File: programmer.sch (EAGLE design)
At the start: 20 parts, among them IC1 74ABT125DB, U1 ATMEGA8U2, X1 16MHz

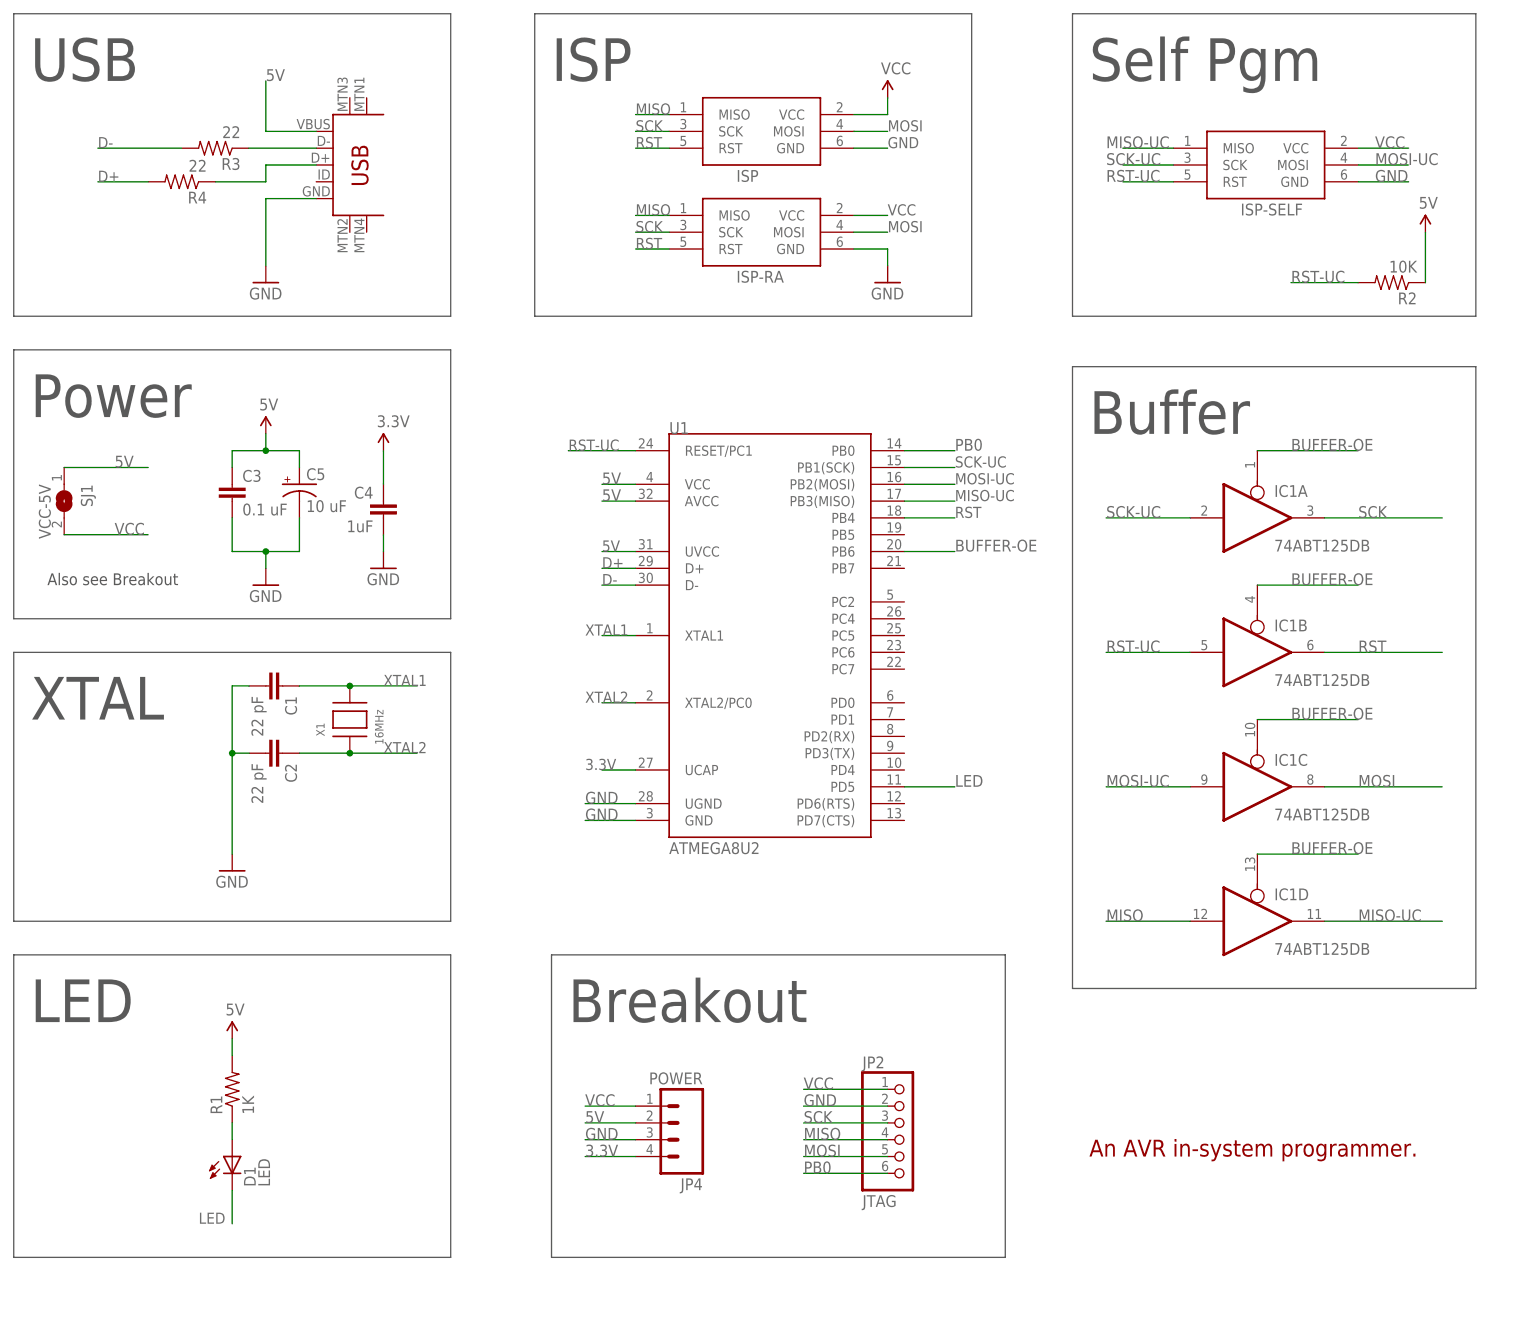
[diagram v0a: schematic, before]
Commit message: Resolved conflicts with dgentry's optimizations.
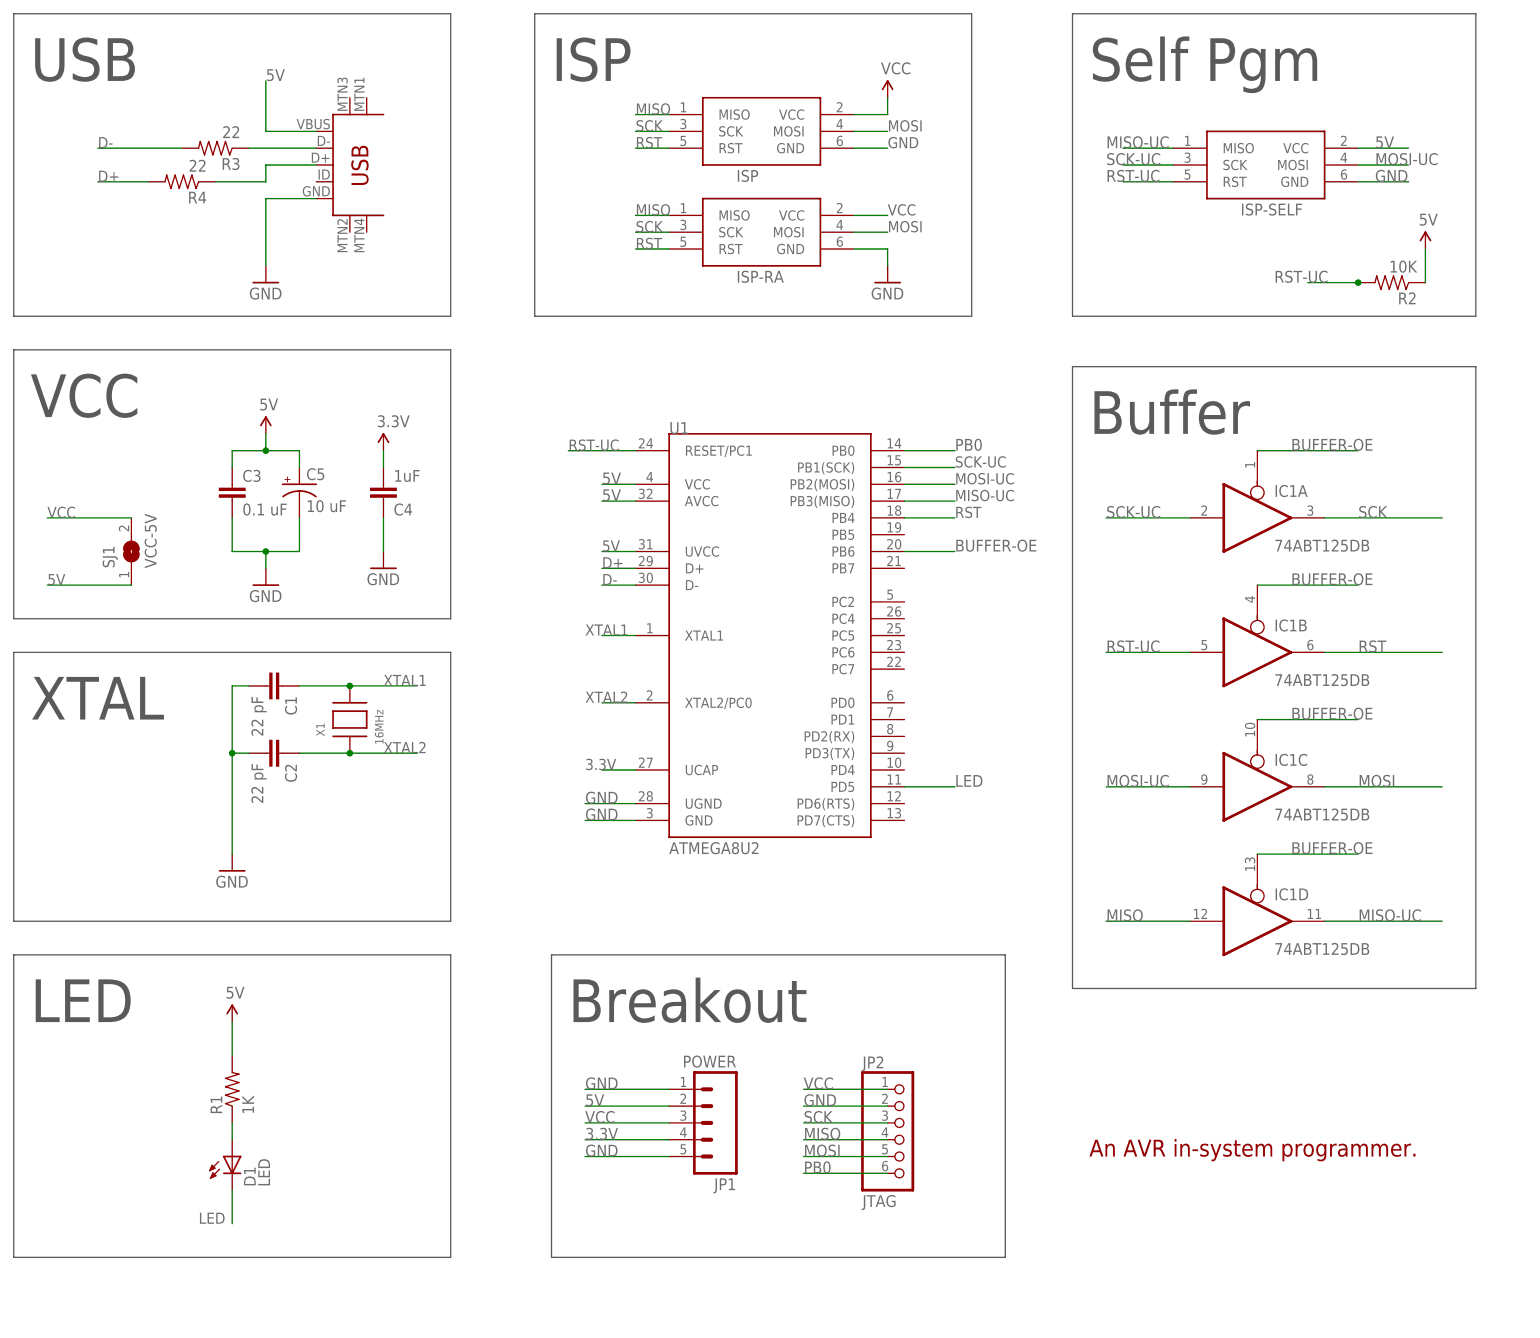
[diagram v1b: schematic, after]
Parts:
- removed JP4: POWER, SparkFun:M04PTH
- added JP1: POWER, SparkFun:M05PTH
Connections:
- net 3.3V: now also C4.2, JP1.4; no longer C4.1, JP4.4
- net 5V: now also ISP-SELF.VCC, JP1.2; no longer JP4.2
- net GND: now also C4.1, JP1.1, JP1.5; no longer C4.2, JP4.3
- net VCC: now also JP1.3; no longer ISP-SELF.VCC, JP4.1
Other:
- note added: "VCC"
- note removed: "Also see Breakout"
- note removed: "Power"
- moved on the sheet: C4, SJ1
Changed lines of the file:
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@@
 <part name="U$2" library="SparkFun" deviceset="5V" device=""/>
 <part name="U$3" library="SparkFun" deviceset="5V" device=""/>
-<part name="JP4" library="SparkFun" deviceset="M04" device="PTH" value="POWER"/>
+<part name="JP1" library="SparkFun" deviceset="M05" device="PTH" value="POWER"/>
 </parts>
 <sheets>
@@
 <wire x1="5.08" y1="48.26" x2="-60.96" y2="48.26" width="0.1524" layer="97"/>
 <wire x1="-60.96" y1="48.26" x2="-60.96" y2="88.9" width="0.1524" layer="97"/>
-<text x="-58.42" y="78.74" size="6.4516" layer="97" font="vector">Power</text>
+<text x="-58.42" y="78.74" size="6.4516" layer="97" font="vector">VCC</text>
 <wire x1="-60.96" y1="43.18" x2="5.08" y2="43.18" width="0.1524" layer="97"/>
 <wire x1="5.08" y1="43.18" x2="5.08" y2="2.54" width="0.1524" layer="97"/>
@@
 <wire x1="20.32" y1="-48.26" x2="20.32" y2="-2.54" width="0.1524" layer="97"/>
 <text x="22.86" y="-12.7" size="6.4516" layer="97" font="vector">Breakout</text>
-<text x="-55.88" y="53.34" size="1.778" layer="97" font="vector">Also see Breakout</text>
 </plain>
 <instances>
@@
 <instance part="R4" gate="G$1" x="-35.56" y="114.3" rot="R180"/>
 <instance part="R3" gate="G$1" x="-30.48" y="119.38" rot="R180"/>
-<instance part="C4" gate="G$1" x="-5.08" y="63.5" rot="MR0"/>
+<instance part="C4" gate="G$1" x="-5.08" y="68.58" rot="MR180"/>
 <instance part="R2" gate="G$1" x="147.32" y="99.06" rot="R180"/>
 <instance part="P+5" gate="G$1" x="-5.08" y="73.66"/>
@@
 <instance part="D1" gate="G$1" x="-27.94" y="-33.02"/>
 <instance part="R1" gate="G$1" x="-27.94" y="-22.86" rot="R90"/>
-<instance part="SJ1" gate="1" x="-53.34" y="66.04" rot="R270"/>
+<instance part="SJ1" gate="1" x="-43.18" y="58.42" rot="R90"/>
 <instance part="C5" gate="G$1" x="-17.78" y="68.58"/>
 <instance part="GND1" gate="1" x="-5.08" y="55.88"/>
@@
 <instance part="JP2" gate="A" x="73.66" y="-30.48"/>
 <instance part="U$1" gate="G$1" x="-22.86" y="76.2"/>
-<instance part="U$2" gate="G$1" x="-27.94" y="-15.24"/>
-<instance part="U$3" gate="G$1" x="152.4" y="106.68"/>
-<instance part="JP4" gate="G$1" x="38.1" y="-27.94" rot="R180"/>
+<instance part="U$2" gate="G$1" x="152.4" y="104.14"/>
+<instance part="U$3" gate="G$1" x="-27.94" y="-12.7"/>
+<instance part="JP1" gate="G$1" x="45.72" y="-27.94" rot="R180"/>
 </instances>
 <busses>
@@
 </segment>
 <segment>
+<wire x1="-55.88" y1="63.5" x2="-43.18" y2="63.5" width="0.1524" layer="91"/>
+<label x="-55.88" y="63.5" size="1.6764" layer="95" font="vector"/>
 <pinref part="SJ1" gate="1" pin="2"/>
-<wire x1="-40.64" y1="60.96" x2="-53.34" y2="60.96" width="0.1524" layer="91"/>
-<label x="-45.72" y="60.96" size="1.778" layer="95" font="vector"/>
-</segment>
-<segment>
-<pinref part="ISP-SELF" gate="G$1" pin="VCC"/>
-<wire x1="142.24" y1="119.38" x2="149.86" y2="119.38" width="0.1524" layer="91"/>
-<label x="144.78" y="119.38" size="1.778" layer="95" font="vector"/>
 </segment>
 <segment>
@@
 </segment>
 <segment>
+<wire x1="38.1" y1="-27.94" x2="25.4" y2="-27.94" width="0.1524" layer="91"/>
+<label x="25.4" y="-27.94" size="1.778" layer="95" font="vector"/>
+<pinref part="JP1" gate="G$1" pin="3"/>
+</segment>
+<segment>
 <pinref part="JP2" gate="A" pin="1"/>
 <wire x1="71.12" y1="-22.86" x2="58.42" y2="-22.86" width="0.1524" layer="91"/>
 <label x="58.42" y="-22.86" size="1.778" layer="95" font="vector"/>
-</segment>
-<segment>
-<pinref part="JP4" gate="G$1" pin="1"/>
-<wire x1="33.02" y1="-25.4" x2="25.4" y2="-25.4" width="0.1524" layer="91"/>
-<label x="25.4" y="-25.4" size="1.778" layer="95" font="vector"/>
 </segment>
 </net>
@@
 </segment>
 <segment>
-<pinref part="C4" gate="G$1" pin="2"/>
+<pinref part="C4" gate="G$1" pin="1"/>
 <pinref part="GND1" gate="1" pin="GND"/>
-<wire x1="-5.08" y1="60.96" x2="-5.08" y2="58.42" width="0.1524" layer="91"/>
+<wire x1="-5.08" y1="63.5" x2="-5.08" y2="58.42" width="0.1524" layer="91"/>
 </segment>
 <segment>
@@
 </segment>
 <segment>
-<pinref part="JP4" gate="G$1" pin="3"/>
-<wire x1="33.02" y1="-30.48" x2="25.4" y2="-30.48" width="0.1524" layer="91"/>
-<label x="25.4" y="-30.48" size="1.778" layer="95" font="vector"/>
-</segment>
-<segment>
+<wire x1="38.1" y1="-33.02" x2="25.4" y2="-33.02" width="0.1524" layer="91"/>
+<label x="25.4" y="-33.02" size="1.778" layer="95" font="vector"/>
+<wire x1="38.1" y1="-22.86" x2="25.4" y2="-22.86" width="0.1524" layer="91"/>
+<label x="25.4" y="-22.86" size="1.778" layer="95" font="vector"/>
+<pinref part="JP1" gate="G$1" pin="1"/>
+<pinref part="JP1" gate="G$1" pin="5"/>
+</segment>
+<segment>
+<pinref part="C5" gate="G$1" pin="-"/>
+<wire x1="-17.78" y1="58.42" x2="-17.78" y2="63.5" width="0.1524" layer="91"/>
 <pinref part="C3" gate="G$1" pin="2"/>
 <wire x1="-27.94" y1="63.5" x2="-27.94" y2="58.42" width="0.1524" layer="91"/>
-<pinref part="C5" gate="G$1" pin="-"/>
 <wire x1="-27.94" y1="58.42" x2="-22.86" y2="58.42" width="0.1524" layer="91"/>
+<pinref part="GND2" gate="1" pin="GND"/>
 <wire x1="-22.86" y1="58.42" x2="-17.78" y2="58.42" width="0.1524" layer="91"/>
-<wire x1="-17.78" y1="58.42" x2="-17.78" y2="63.5" width="0.1524" layer="91"/>
-<pinref part="GND2" gate="1" pin="GND"/>
 <wire x1="-22.86" y1="58.42" x2="-22.86" y2="55.88" width="0.1524" layer="91"/>
 <junction x="-22.86" y="58.42"/>
@@
 <net name="3.3V" class="0">
 <segment>
-<pinref part="C4" gate="G$1" pin="1"/>
+<pinref part="C4" gate="G$1" pin="2"/>
 <pinref part="P+5" gate="G$1" pin="3.3V"/>
-<wire x1="-5.08" y1="68.58" x2="-5.08" y2="73.66" width="0.1524" layer="91"/>
+<wire x1="-5.08" y1="71.12" x2="-5.08" y2="73.66" width="0.1524" layer="91"/>
 </segment>
 <segment>
@@
 </segment>
 <segment>
-<pinref part="JP4" gate="G$1" pin="4"/>
-<wire x1="33.02" y1="-33.02" x2="25.4" y2="-33.02" width="0.1524" layer="91"/>
-<label x="25.4" y="-33.02" size="1.778" layer="95" font="vector"/>
+<wire x1="38.1" y1="-30.48" x2="25.4" y2="-30.48" width="0.1524" layer="91"/>
+<label x="25.4" y="-30.48" size="1.778" layer="95" font="vector"/>
+<pinref part="JP1" gate="G$1" pin="4"/>
 </segment>
 </net>
@@
 </segment>
 <segment>
-<wire x1="-40.64" y1="71.12" x2="-53.34" y2="71.12" width="0.1524" layer="91"/>
+<label x="-55.88" y="53.34" size="1.6764" layer="95" font="vector"/>
+<wire x1="-55.88" y1="53.34" x2="-43.18" y2="53.34" width="0.1524" layer="91"/>
 <pinref part="SJ1" gate="1" pin="1"/>
-<label x="-45.72" y="71.12" size="1.778" layer="95" font="vector"/>
 </segment>
 <segment>
 <pinref part="U1" gate="G$1" pin="VCC"/>
 <wire x1="33.02" y1="68.58" x2="27.94" y2="68.58" width="0.1524" layer="91"/>
-<label x="27.94" y="68.58" size="1.778" layer="95"/>
+<label x="27.94" y="68.58" size="1.778" layer="95" font="vector"/>
 </segment>
 <segment>
 <pinref part="U1" gate="G$1" pin="AVCC"/>
 <wire x1="33.02" y1="66.04" x2="27.94" y2="66.04" width="0.1524" layer="91"/>
-<label x="27.94" y="66.04" size="1.778" layer="95"/>
+<label x="27.94" y="66.04" size="1.778" layer="95" font="vector"/>
 </segment>
 <segment>
@@
 <wire x1="-27.94" y1="71.12" x2="-27.94" y2="73.66" width="0.1524" layer="91"/>
 <wire x1="-27.94" y1="73.66" x2="-22.86" y2="73.66" width="0.1524" layer="91"/>
-<pinref part="U$1" gate="G$1" pin="5V"/>
 <wire x1="-22.86" y1="73.66" x2="-17.78" y2="73.66" width="0.1524" layer="91"/>
 <wire x1="-22.86" y1="76.2" x2="-22.86" y2="73.66" width="0.1524" layer="91"/>
 <junction x="-22.86" y="73.66"/>
-</segment>
-<segment>
+<pinref part="U$1" gate="G$1" pin="5V"/>
+</segment>
+<segment>
+<pinref part="R2" gate="G$1" pin="1"/>
+<wire x1="152.4" y1="99.06" x2="152.4" y2="104.14" width="0.1524" layer="91"/>
 <pinref part="U$2" gate="G$1" pin="5V"/>
+</segment>
+<segment>
 <pinref part="R1" gate="G$1" pin="2"/>
-<wire x1="-27.94" y1="-15.24" x2="-27.94" y2="-17.78" width="0.1524" layer="91"/>
-</segment>
-<segment>
+<wire x1="-27.94" y1="-12.7" x2="-27.94" y2="-17.78" width="0.1524" layer="91"/>
 <pinref part="U$3" gate="G$1" pin="5V"/>
-<pinref part="R2" gate="G$1" pin="1"/>
-<wire x1="152.4" y1="106.68" x2="152.4" y2="99.06" width="0.1524" layer="91"/>
-</segment>
-<segment>
-<pinref part="JP4" gate="G$1" pin="2"/>
-<wire x1="33.02" y1="-27.94" x2="25.4" y2="-27.94" width="0.1524" layer="91"/>
-<label x="25.4" y="-27.94" size="1.778" layer="95" font="vector"/>
+</segment>
+<segment>
+<wire x1="25.4" y1="-25.4" x2="38.1" y2="-25.4" width="0.1524" layer="91"/>
+<label x="25.4" y="-25.4" size="1.778" layer="95" font="vector"/>
+<pinref part="JP1" gate="G$1" pin="2"/>
+</segment>
+<segment>
+<pinref part="ISP-SELF" gate="G$1" pin="VCC"/>
+<wire x1="142.24" y1="119.38" x2="149.86" y2="119.38" width="0.1524" layer="91"/>
+<label x="144.78" y="119.38" size="1.778" layer="95" font="vector"/>
 </segment>
 </net>
@@
 </segment>
 <segment>
+<pinref part="R2" gate="G$1" pin="2"/>
+<label x="129.54" y="99.06" size="1.778" layer="95" font="vector"/>
+<wire x1="142.24" y1="99.06" x2="134.62" y2="99.06" width="0.1524" layer="91"/>
+<junction x="142.24" y="99.06"/>
+</segment>
+<segment>
 <pinref part="ISP-SELF" gate="G$1" pin="RST"/>
 <wire x1="114.3" y1="114.3" x2="106.68" y2="114.3" width="0.1524" layer="91"/>
@@
 <label x="104.14" y="43.18" size="1.778" layer="95" font="vector"/>
 </segment>
-<segment>
-<pinref part="R2" gate="G$1" pin="2"/>
-<wire x1="142.24" y1="99.06" x2="132.08" y2="99.06" width="0.1524" layer="91"/>
-<label x="132.08" y="99.06" size="1.778" layer="95" font="vector"/>
-</segment>
-</net>
+</net>

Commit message: Fixed: PB0 replaced with RST for JTAG header.
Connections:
- removed net PB0: JP2.6, U1.PB0
- net RST: now also JP2.6
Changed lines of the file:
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@@
 <label x="142.24" y="43.18" size="1.778" layer="95" font="vector"/>
+</segment>
+<segment>
+<pinref part="JP2" gate="A" pin="6"/>
+<wire x1="71.12" y1="-35.56" x2="58.42" y2="-35.56" width="0.1524" layer="91"/>
+<label x="58.42" y="-35.56" size="1.778" layer="95"/>
 </segment>
 </net>
@@
 </segment>
 </net>
-<net name="PB0" class="0">
-<segment>
-<pinref part="JP2" gate="A" pin="6"/>
-<wire x1="71.12" y1="-35.56" x2="58.42" y2="-35.56" width="0.1524" layer="91"/>
-<label x="58.42" y="-35.56" size="1.778" layer="95" font="vector"/>
-</segment>
-<segment>
-<pinref part="U1" gate="G$1" pin="PB0"/>
-<wire x1="73.66" y1="73.66" x2="81.28" y2="73.66" width="0.1524" layer="91"/>
-<label x="81.28" y="73.66" size="1.778" layer="95" font="vector"/>
-</segment>
-</net>
